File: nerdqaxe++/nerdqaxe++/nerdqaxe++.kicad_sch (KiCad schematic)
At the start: 9 parts, among them J1 XT30

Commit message: Powermining revision
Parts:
- added F1: Fuseholder_Blade_Mini_Keystone_3568, 8Axe:Fuseholder Blade_3568, symbol Fuseholder Blade 3568:3568
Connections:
- net Power/+12V: now also F1.2; no longer J1.1 (+V)
- new net: F1.1, J1.1 (+V)
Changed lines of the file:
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@@
 	)
 	(junction
-		(at 55.245 52.07)
+		(at 60.96 52.07)
 		(diameter 0)
 		(color 0 0 0 0)
@@
 	(wire
 		(pts
-			(xy 33.02 52.07) (xy 55.245 52.07)
-		)
-		(stroke
-			(width 0)
-			(type default)
-		)
-	)
-	(wire
-		(pts
-			(xy 55.245 54.61) (xy 55.245 52.07)
+			(xy 60.96 54.61) (xy 60.96 52.07)
 		)
 		(stroke
@@
 	(wire
 		(pts
-			(xy 55.245 66.675) (xy 55.245 62.23)
+			(xy 60.96 62.23) (xy 60.96 67.31)
 		)
 		(stroke
@@
 	(wire
 		(pts
+			(xy 57.15 52.07) (xy 60.96 52.07)
+		)
+		(stroke
+			(width 0)
+			(type default)
+		)
+	)
+	(wire
+		(pts
 			(xy 99.695 57.785) (xy 114.3 57.785)
 		)
@@
 	(wire
 		(pts
+			(xy 33.02 52.07) (xy 41.91 52.07)
+		)
+		(stroke
+			(width 0)
+			(type default)
+		)
+	)
+	(wire
+		(pts
 			(xy 75.565 84.455) (xy 75.565 97.79)
 		)
@@
 	(wire
 		(pts
+			(xy 60.96 52.07) (xy 77.47 52.07)
+		)
+		(stroke
+			(width 0)
+			(type default)
+		)
+	)
+	(wire
+		(pts
 			(xy 99.695 55.88) (xy 113.03 55.88)
 		)
@@
 		(pts
 			(xy 123.19 66.04) (xy 123.19 94.615)
-		)
-		(stroke
-			(width 0)
-			(type default)
-		)
-	)
-	(wire
-		(pts
-			(xy 55.245 52.07) (xy 77.47 52.07)
 		)
 		(stroke
@@
 	(symbol
 		(lib_id "power:GND")
-		(at 55.245 66.675 0)
+		(at 60.96 67.31 0)
 		(unit 1)
 		(exclude_from_sim no)
@@
 		(dnp no)
 		(property "Reference" "#PWR04"
-			(at 55.245 73.025 0)
+			(at 60.96 73.66 0)
 			(effects
 				(font
@@
 		)
 		(property "Value" "GND"
-			(at 55.372 71.0692 0)
+			(at 61.087 71.7042 0)
 			(effects
 				(font
@@
 		)
 		(property "Footprint" ""
-			(at 55.245 66.675 0)
+			(at 60.96 67.31 0)
 			(effects
 				(font
@@
 		)
 		(property "Datasheet" ""
-			(at 55.245 66.675 0)
+			(at 60.96 67.31 0)
 			(effects
 				(font
@@
 		)
 		(property "Description" ""
-			(at 55.245 66.675 0)
+			(at 60.96 67.31 0)
 			(effects
 				(font
@@
 	(symbol
 		(lib_id "Diode:5KPxxA")
-		(at 55.245 58.42 270)
+		(at 60.96 58.42 270)
 		(unit 1)
 		(exclude_from_sim no)
@@
 		(dnp no)
 		(property "Reference" "D1"
-			(at 52.324 57.15 0)
+			(at 58.039 57.15 0)
 			(effects
 				(font
@@
 		)
 		(property "Value" "5KPxxA"
-			(at 58.166 58.42 0)
+			(at 63.881 58.42 0)
 			(effects
 				(font
@@
 		)
 		(property "Footprint" "Diode_SMD:D_SMB"
-			(at 50.165 58.42 0)
+			(at 55.88 58.42 0)
 			(effects
 				(font
@@
 		)
 		(property "Datasheet" "https://diotec.com/tl_files/diotec/files/pdf/datasheets/5kp65.pdf"
-			(at 55.245 57.15 0)
+			(at 60.96 57.15 0)
 			(effects
 				(font
@@
 		)
 		(property "Description" "5000W unidirectional Transient Voltage Suppressor, P-600"
-			(at 55.245 58.42 0)
+			(at 60.96 58.42 0)
 			(effects
 				(font
@@
 		)
 		(property "Distributor" "D"
-			(at 55.245 58.42 0)
+			(at 60.96 58.42 0)
 			(effects
 				(font
@@
 		)
 		(property "OrderNr" "SMBJ12ALFCT-ND"
-			(at 55.245 58.42 0)
+			(at 60.96 58.42 0)
 			(effects
 				(font
@@
 		)
 		(property "PARTNO" "SMBJ12A"
-			(at 55.245 58.42 0)
+			(at 60.96 58.42 0)
 			(effects
 				(font
@@
 		)
 		(property "Manufacturer " "UMW(Youtai Semiconductor Co., Ltd.)"
-			(at 55.245 58.42 0)
+			(at 60.96 58.42 0)
 			(effects
 				(font
@@
 		)
 		(property "LCSC" "C3001973"
-			(at 55.245 58.42 0)
+			(at 60.96 58.42 0)
 			(effects
 				(font
@@
 					(unit 1)
 				)
+			)
+		)
+	)
+	(symbol
+		(lib_id "Fuseholder Blade 3568:3568")
+		(at 49.53 52.07 0)
+		(unit 1)
+		(exclude_from_sim no)
+		(in_bom yes)
+		(on_board yes)
+		(dnp no)
+		(fields_autoplaced yes)
+		(property "Reference" "F1"
+			(at 49.53 45.466 0)
+			(effects
+				(font
+					(size 1.27 1.27)
+				)
+			)
+		)
+		(property "Value" "Fuseholder_Blade_Mini_Keystone_3568"
+			(at 49.53 48.006 0)
+			(effects
+				(font
+					(size 1.27 1.27)
+				)
+			)
+		)
+		(property "Footprint" "8Axe:Fuseholder Blade_3568"
+			(at 49.53 52.07 0)
+			(effects
+				(font
+					(size 1.27 1.27)
+				)
+				(justify bottom)
+				(hide yes)
+			)
+		)
+		(property "Datasheet" ""
+			(at 49.53 52.07 0)
+			(effects
+				(font
+					(size 1.27 1.27)
+				)
+				(hide yes)
+			)
+		)
+		(property "Description" "Fuseholder Mini Blade"
+			(at 49.53 52.07 0)
+			(effects
+				(font
+					(size 1.27 1.27)
+				)
+				(hide yes)
+			)
+		)
+		(property "Manufacturer" "3568"
+			(at 49.53 52.07 0)
+			(effects
+				(font
+					(size 1.27 1.27)
+				)
+				(justify bottom)
+				(hide yes)
+			)
+		)
+		(property "Distributor" "D"
+			(at 49.53 52.07 0)
+			(effects
+				(font
+					(size 1.27 1.27)
+				)
+				(hide yes)
+			)
+		)
+		(property "OrderNr" "36-3568-ND"
+			(at 49.53 52.07 0)
+			(effects
+				(font
+					(size 1.27 1.27)
+				)
+				(hide yes)
+			)
+		)
+		(pin "1"
+		)
+		(pin "2"
+		)
+		(instances
+			(project "nerdqaxe++"
+				(path "/e63e39d7-6ac0-4ffd-8aa3-1841a4541b55"
+					(reference "F1")
+					(unit 1)
+				)

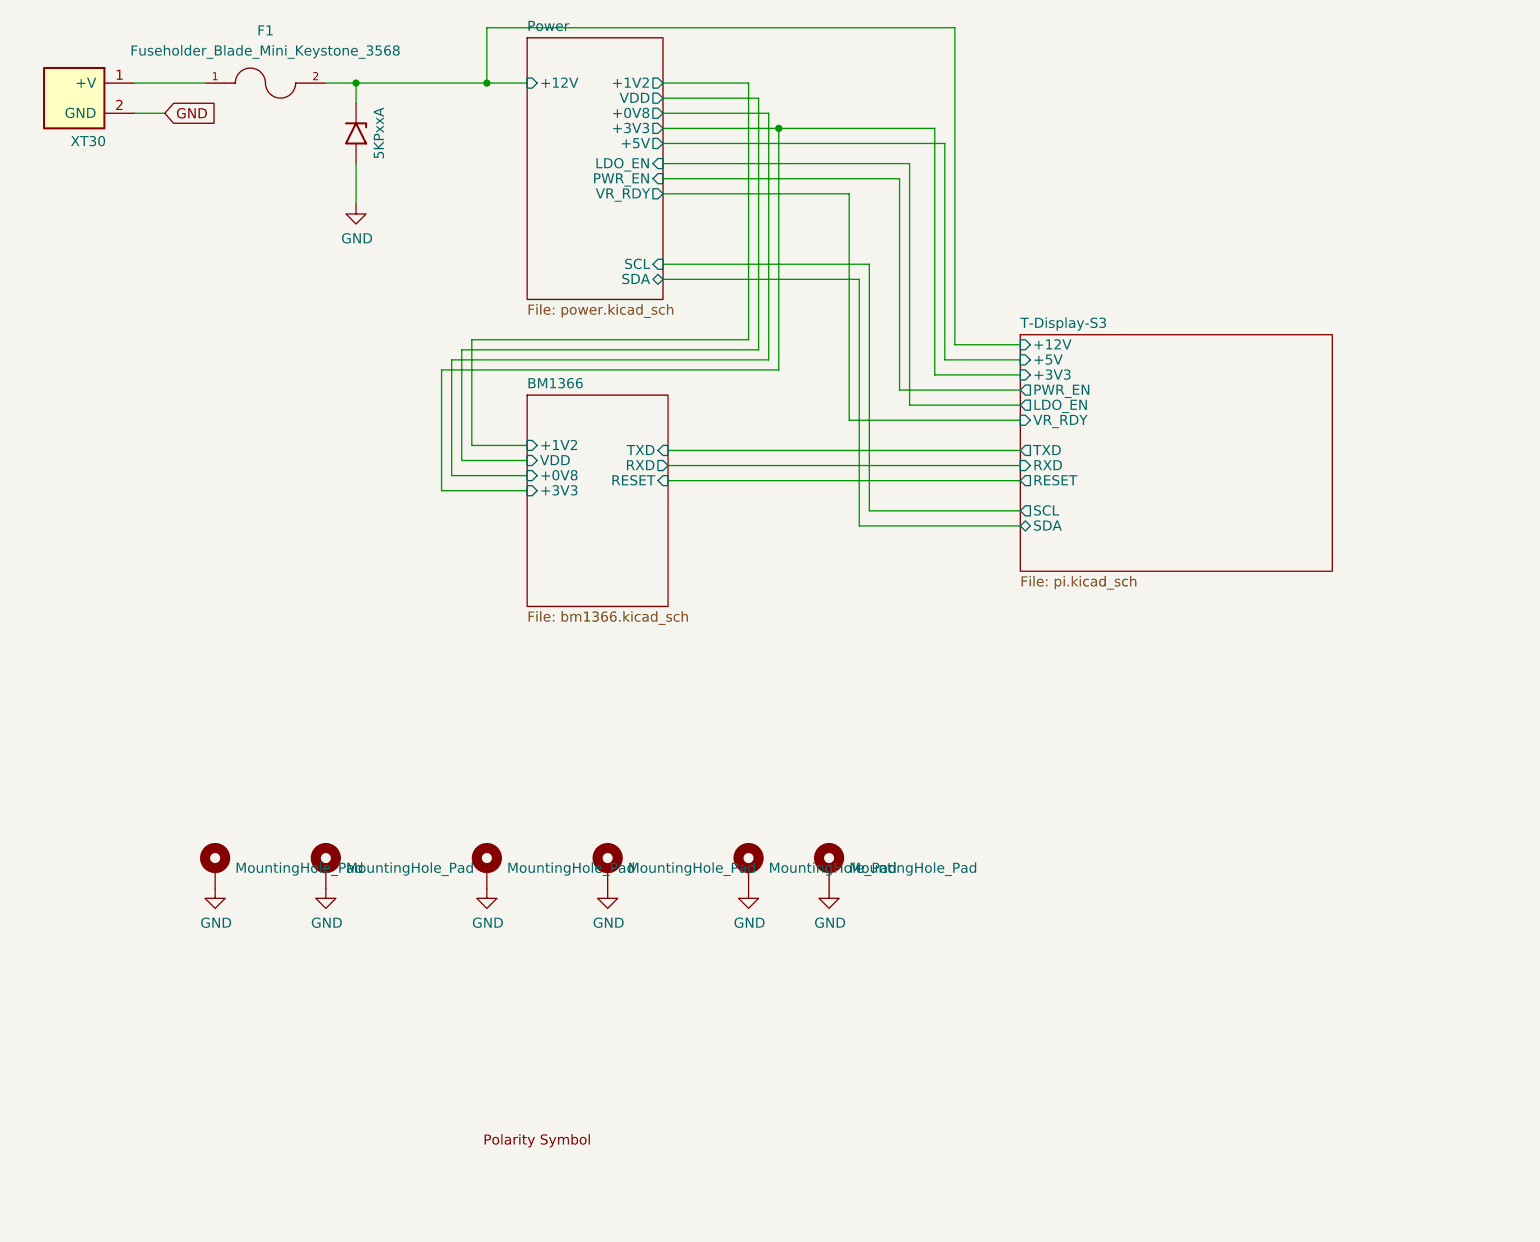
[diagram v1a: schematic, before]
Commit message: Edit on rev 6.1PM
- Moved XT30 connector to the back of the board
- Edited VDD polygon
- Fixed various via placements
- Fixed various tracing
- Updated BM1370 footprint and solder paste stencil
- Updated CSD95472Q5MC footprint and solder paste stencil
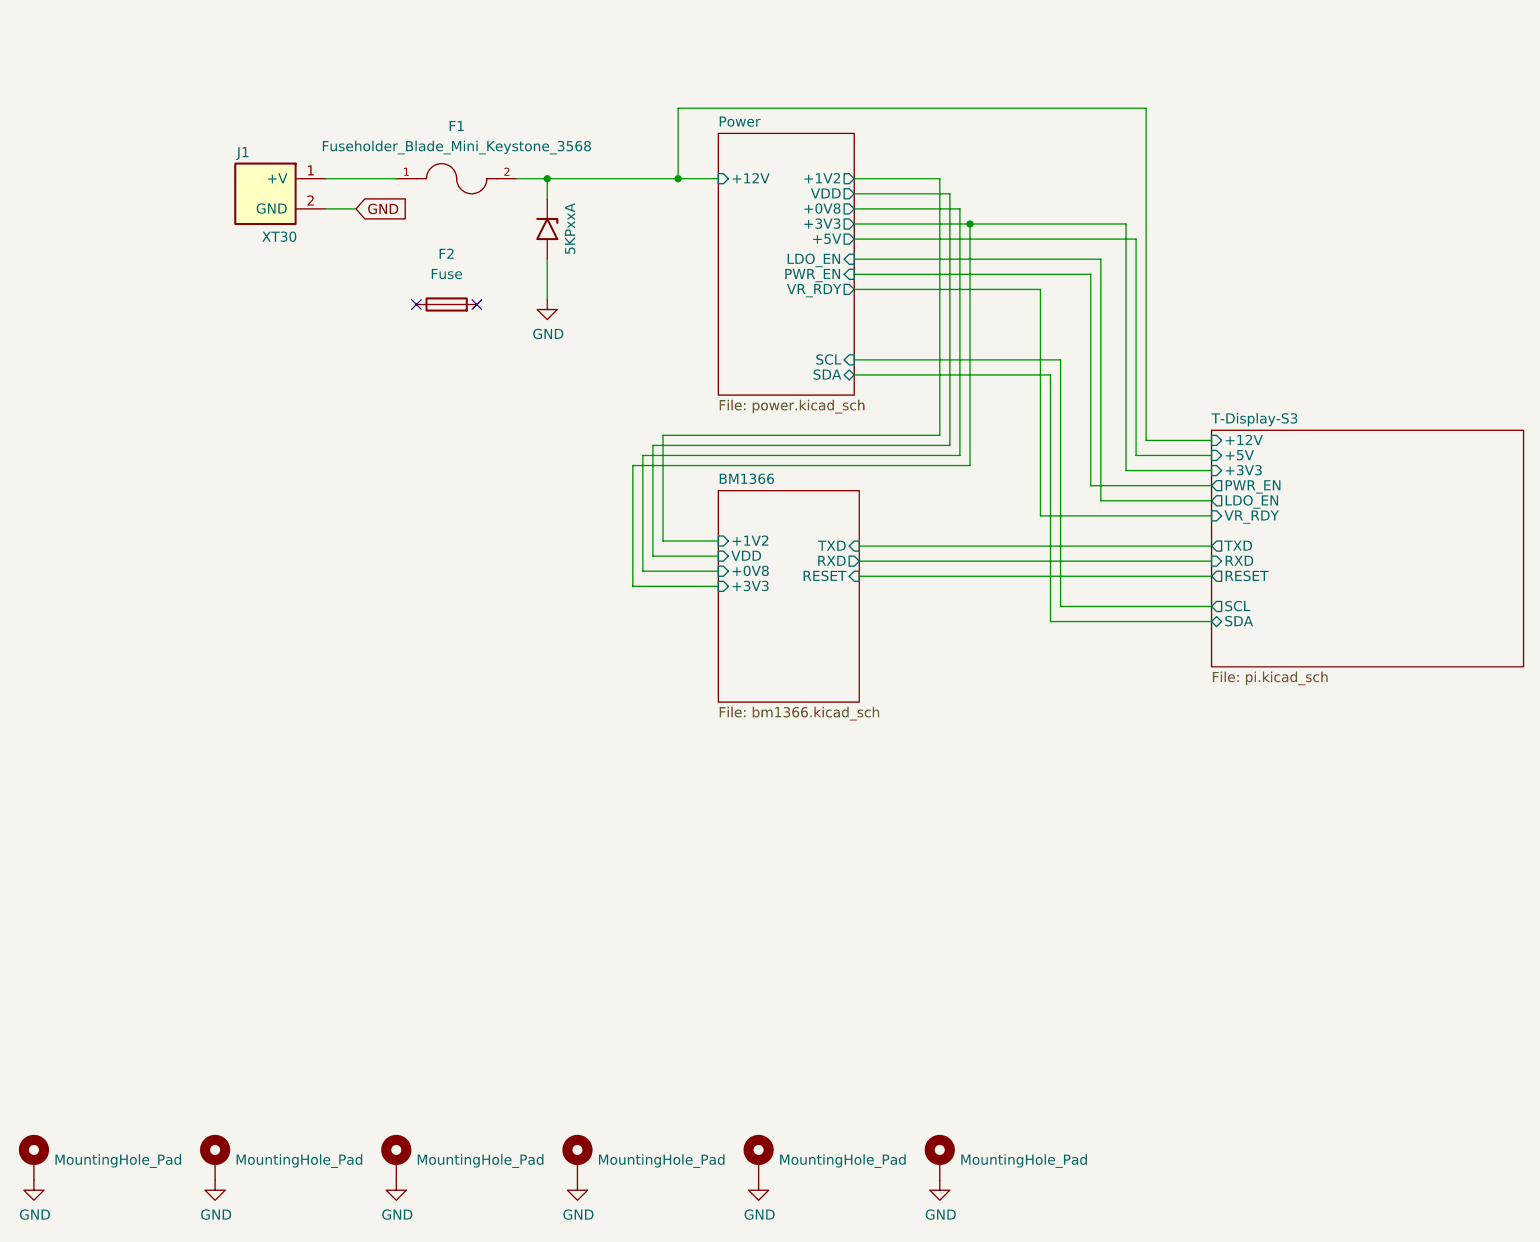
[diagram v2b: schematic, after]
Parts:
- removed U1: ~, bitaxe:polarity, symbol bitaxe:polarity
- added F2: Fuse, symbol Device:Fuse
- F1: LCSC (none) -> C5249699; Manufacturer 3568 -> (none); Manufacturer  (none) -> Keystone; PARTNO (none) -> 3568
- J1: Manufacturer  (none) -> Changzhou Amass Elec
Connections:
- no-connect marks 0 -> 2
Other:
- moved on the sheet: F1
